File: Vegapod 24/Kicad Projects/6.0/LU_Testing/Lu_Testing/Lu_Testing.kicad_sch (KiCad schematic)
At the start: 101 parts, among them J1 DC Link, J2 OUT, J3 17V-35V IN, Q1 Q_NMOS_GDS, Q2 Q_NMOS_GDS, Q3 Q_PMOS_GSD, Q4 Q_PMOS_GSD, Q5 Q_PMOS_GSD, U1 LM7815_TO220, U2 KA78M05_TO252, U3 IR2110, U4 B0505S-1WR3, U5 LM324, U6 6N137, U7 6N137, U8 6N137

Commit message: LU PCB
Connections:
- net at C32.2, R37.1: now also U5.9 (-); no longer U5.6 (-)
- net at U5.10 (+): now also R38.1
- net at U5.5 (+): no longer R38.1
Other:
- moved on the sheet: U5B, U5C, U5D
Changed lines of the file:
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@@
+    (stroke (width 0) (type default) (color 0 0 0 0))
+  )
+  (wire (pts (xy 48.26 134.62) (xy 48.26 135.89))
     (stroke (width 0) (type default) (color 0 0 0 0))
   )
@@
     (stroke (width 0) (type default) (color 0 0 0 0))
   )
-  (wire (pts (xy 48.26 137.16) (xy 48.26 134.62))
-    (stroke (width 0) (type default) (color 0 0 0 0))
-  )
   (wire (pts (xy 38.1 156.21) (xy 34.29 156.21))
     (stroke (width 0) (type default) (color 0 0 0 0))
@@
   )
   (wire (pts (xy 173.99 67.31) (xy 173.99 74.93))
+    (stroke (width 0) (type default) (color 0 0 0 0))
+  )
+  (wire (pts (xy 48.26 132.08) (xy 48.26 130.81))
     (stroke (width 0) (type default) (color 0 0 0 0))
   )
@@
     (pin "2")
   )
-  (symbol (lib_id "Amplifier_Operational:LM324") (at 74.93 146.05 0) (unit 3)
-    (in_bom yes) (on_board yes) (fields_autoplaced)
-    (property "Reference" "U5" (id 0) (at 74.93 135.89 0))
-    (property "Value" "LM324" (id 1) (at 74.93 138.43 0))
-    (property "Footprint" "Package_SO:SOIC-14_3.9x8.7mm_P1.27mm" (id 2) (at 73.66 143.51 0)
-      (effects (font (size 1.27 1.27)) hide)
-    )
-    (property "Datasheet" "http://www.ti.com/lit/ds/symlink/lm2902-n.pdf" (id 3) (at 76.2 140.97 0)
+  (symbol (lib_id "Amplifier_Operational:LM324") (at 55.88 133.35 0) (unit 3)
+    (in_bom yes) (on_board yes) (fields_autoplaced)
+    (property "Reference" "U5" (id 0) (at 55.88 123.19 0))
+    (property "Value" "LM324" (id 1) (at 55.88 125.73 0))
+    (property "Footprint" "Package_SO:SOIC-14_3.9x8.7mm_P1.27mm" (id 2) (at 54.61 130.81 0)
+      (effects (font (size 1.27 1.27)) hide)
+    )
+    (property "Datasheet" "http://www.ti.com/lit/ds/symlink/lm2902-n.pdf" (id 3) (at 57.15 128.27 0)
       (effects (font (size 1.27 1.27)) hide)
     )
@@
     (pin "2")
   )
-  (symbol (lib_id "Amplifier_Operational:LM324") (at 100.33 139.7 0) (unit 4)
-    (in_bom yes) (on_board yes) (fields_autoplaced)
-    (property "Reference" "U5" (id 0) (at 100.33 129.54 0))
-    (property "Value" "LM324" (id 1) (at 100.33 132.08 0))
-    (property "Footprint" "Package_SO:SOIC-14_3.9x8.7mm_P1.27mm" (id 2) (at 99.06 137.16 0)
-      (effects (font (size 1.27 1.27)) hide)
-    )
-    (property "Datasheet" "http://www.ti.com/lit/ds/symlink/lm2902-n.pdf" (id 3) (at 101.6 134.62 0)
+  (symbol (lib_id "Amplifier_Operational:LM324") (at 85.09 133.35 0) (unit 4)
+    (in_bom yes) (on_board yes) (fields_autoplaced)
+    (property "Reference" "U5" (id 0) (at 85.09 123.19 0))
+    (property "Value" "LM324" (id 1) (at 85.09 125.73 0))
+    (property "Footprint" "Package_SO:SOIC-14_3.9x8.7mm_P1.27mm" (id 2) (at 83.82 130.81 0)
+      (effects (font (size 1.27 1.27)) hide)
+    )
+    (property "Datasheet" "http://www.ti.com/lit/ds/symlink/lm2902-n.pdf" (id 3) (at 86.36 128.27 0)
       (effects (font (size 1.27 1.27)) hide)
     )
@@
     (pin "2")
   )
-  (symbol (lib_id "Amplifier_Operational:LM324") (at 55.88 134.62 0) (unit 2)
-    (in_bom yes) (on_board yes) (fields_autoplaced)
-    (property "Reference" "U5" (id 0) (at 55.88 124.46 0))
-    (property "Value" "LM324" (id 1) (at 55.88 127 0))
-    (property "Footprint" "Package_SO:SOIC-14_3.9x8.7mm_P1.27mm" (id 2) (at 54.61 132.08 0)
-      (effects (font (size 1.27 1.27)) hide)
-    )
-    (property "Datasheet" "http://www.ti.com/lit/ds/symlink/lm2902-n.pdf" (id 3) (at 57.15 129.54 0)
-      (effects (font (size 1.27 1.27)) hide)
-    )
+  (symbol (lib_id "Amplifier_Operational:LM324") (at 31.75 123.19 0) (unit 2)
+    (in_bom yes) (on_board yes) (fields_autoplaced)
+    (property "Reference" "U5" (id 0) (at 31.75 113.03 0))
+    (property "Value" "LM324" (id 1) (at 31.75 115.57 0))
+    (property "Footprint" "Package_SO:SOIC-14_3.9x8.7mm_P1.27mm" (id 2) (at 30.48 120.65 0)
+      (effects (font (size 1.27 1.27)) hide)
+    )
+    (property "Datasheet" "http://www.ti.com/lit/ds/symlink/lm2902-n.pdf" (id 3) (at 33.02 118.11 0)
+      (effects (font (size 1.27 1.27)) hide)
+    )

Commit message: Power side complete lu
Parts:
- added C33, C34, C35, C37, C38: 100n, Capacitor_SMD:C_0805_2012Metric_Pad1.18x1.45mm_HandSolder, symbol Device:C_Small
- added C36, C39: 10u, Capacitor_SMD:C_1206_3216Metric_Pad1.33x1.80mm_HandSolder, symbol Device:C_Small
- added U10: ADUM4195-1BRIZ, ADUM4195-1:RI-8-1_ADI, symbol ADUM4195-1:ADUM4195-1BRIZ
- added U9: 6N137, Package_DIP:DIP-8_W7.62mm, symbol Isolator:6N137
- renumbered C11 to C1, C20 to C10, C5 to C11, C10 to C12, C8 to C13, C13 to C14, C17 to C15, C21 to C16, C6 to C17, C24 to C18, C14 to C19, C12 to C2, C1 to C20, C25 to C21, C2 to C23, C3 to C24, C23 to C25, C31 to C26, C26 to C27, C27 to C28, C28 to C29, C18 to C3, C29 to C30, C30 to C31, C9 to C5, C15 to C6, C19 to C7, C7 to C8, C16 to C9, D5 to D1, D6 to D2, D1 to D3, D8 to D4, D2 to D5, D4 to D6, D3 to D7, D7 to D8, J3 to J2, J2 to J3, R10 to R1, R20 to R10, R4 to R11, R26 to R12, R21 to R13, R28 to R14, R29 to R15, R30 to R16, R23 to R17, R1 to R18, R2 to R19, R13 to R2, R5 to R20, R6 to R21, R7 to R22, R8 to R23, R9 to R24, R12 to R25, R15 to R26, R18 to R27, R27 to R28, R24 to R29, R16 to R3, R39 to R30, R25 to R31, R40 to R32, R38 to R33, R37 to R34, R31 to R35, R34 to R36, R32 to R37, R35 to R38, R33 to R39, R19 to R4, R36 to R40, R22 to R5, R11 to R6, R14 to R7, R17 to R8, R3 to R9, U2 to U1, U1 to U2, U4 to U3, U3 to U4
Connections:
- net +5V: now also C33.1, C34.1, C35.1, C36.2, C37.2, U10.1 (VDD2)
- net A0: now also U10.2 (VIN)
- net GNDPWR: now also C33.2, C34.2, C35.2, C36.1, C37.1, U10.3 (SHTD), U10.4 (GND2), U9.3 (C)
- net CO: now reaches U5.8
- net CO: now also U9.2 (A)
- new net: C38.2, C39.2, U10.5 (GND1), U10.6 (NC)
- new net: C38.1, C39.1, U10.8 (VDD1)

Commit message: LU testing board
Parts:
- added C35: 47n, Capacitor_SMD:C_0805_2012Metric_Pad1.18x1.45mm_HandSolder, symbol Device:C_Small
- added R39: 220, Resistor_SMD:R_0805_2012Metric_Pad1.20x1.40mm_HandSolder, symbol Device:R
- added U9: STM32G474RET6, STM32G4:QFP50P1200X1200X160-64N, symbol STM32G4:STM32G474RET6
- renumbered C35 to C36, C36 to C37, C37 to C38, C38 to C39, C39 to C40, R39 to R40, R40 to R41, U9 to U10, U10 to U11
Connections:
- net DHIN: now reaches U7.2 (A)
- net DHIN: now also U9.8 (PC0)
- net GNDD: now reaches U7.3 (C)
- net GNDD: now also C39.2, C40.2, U10.5 (GND), U11.5 (GND1), U11.6 (NC), U6.3 (C), U8.3 (C), C35.1, U9.15 (VSS), U9.27 (VSSA), U9.31 (VSS), U9.47 (VSS), U9.63 (VSS)
- net DA0: now reaches U11.7 (VOUT)
- net DA0: now also U9.12 (PA0)
- net +5VD: now reaches C39.1, C40.1, U11.8 (VDD1)
- net +5VD: now also U10.7 (EN), U10.8 (VCC)
- net DPWMADJ: now reaches U6.2 (A)
- net DPWMADJ: now also U9.20 (PA6)
- net DLIN: now reaches U8.2 (A)
- net DLIN: now also U9.2 (PC13)
- net DFB: now reaches U10.6 (VO)
- net DFB: now also U9.24 (PB0)
- new net: C35.2, R39.1, U9.29 (VDDA)
- new net +3.3V: R39.2, U9.1 (VBAT), U9.16 (VDD), U9.32 (VDD), U9.48 (VDD), U9.64 (VDD)
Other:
- moved on the sheet: C37, C38, C39, C40, U11

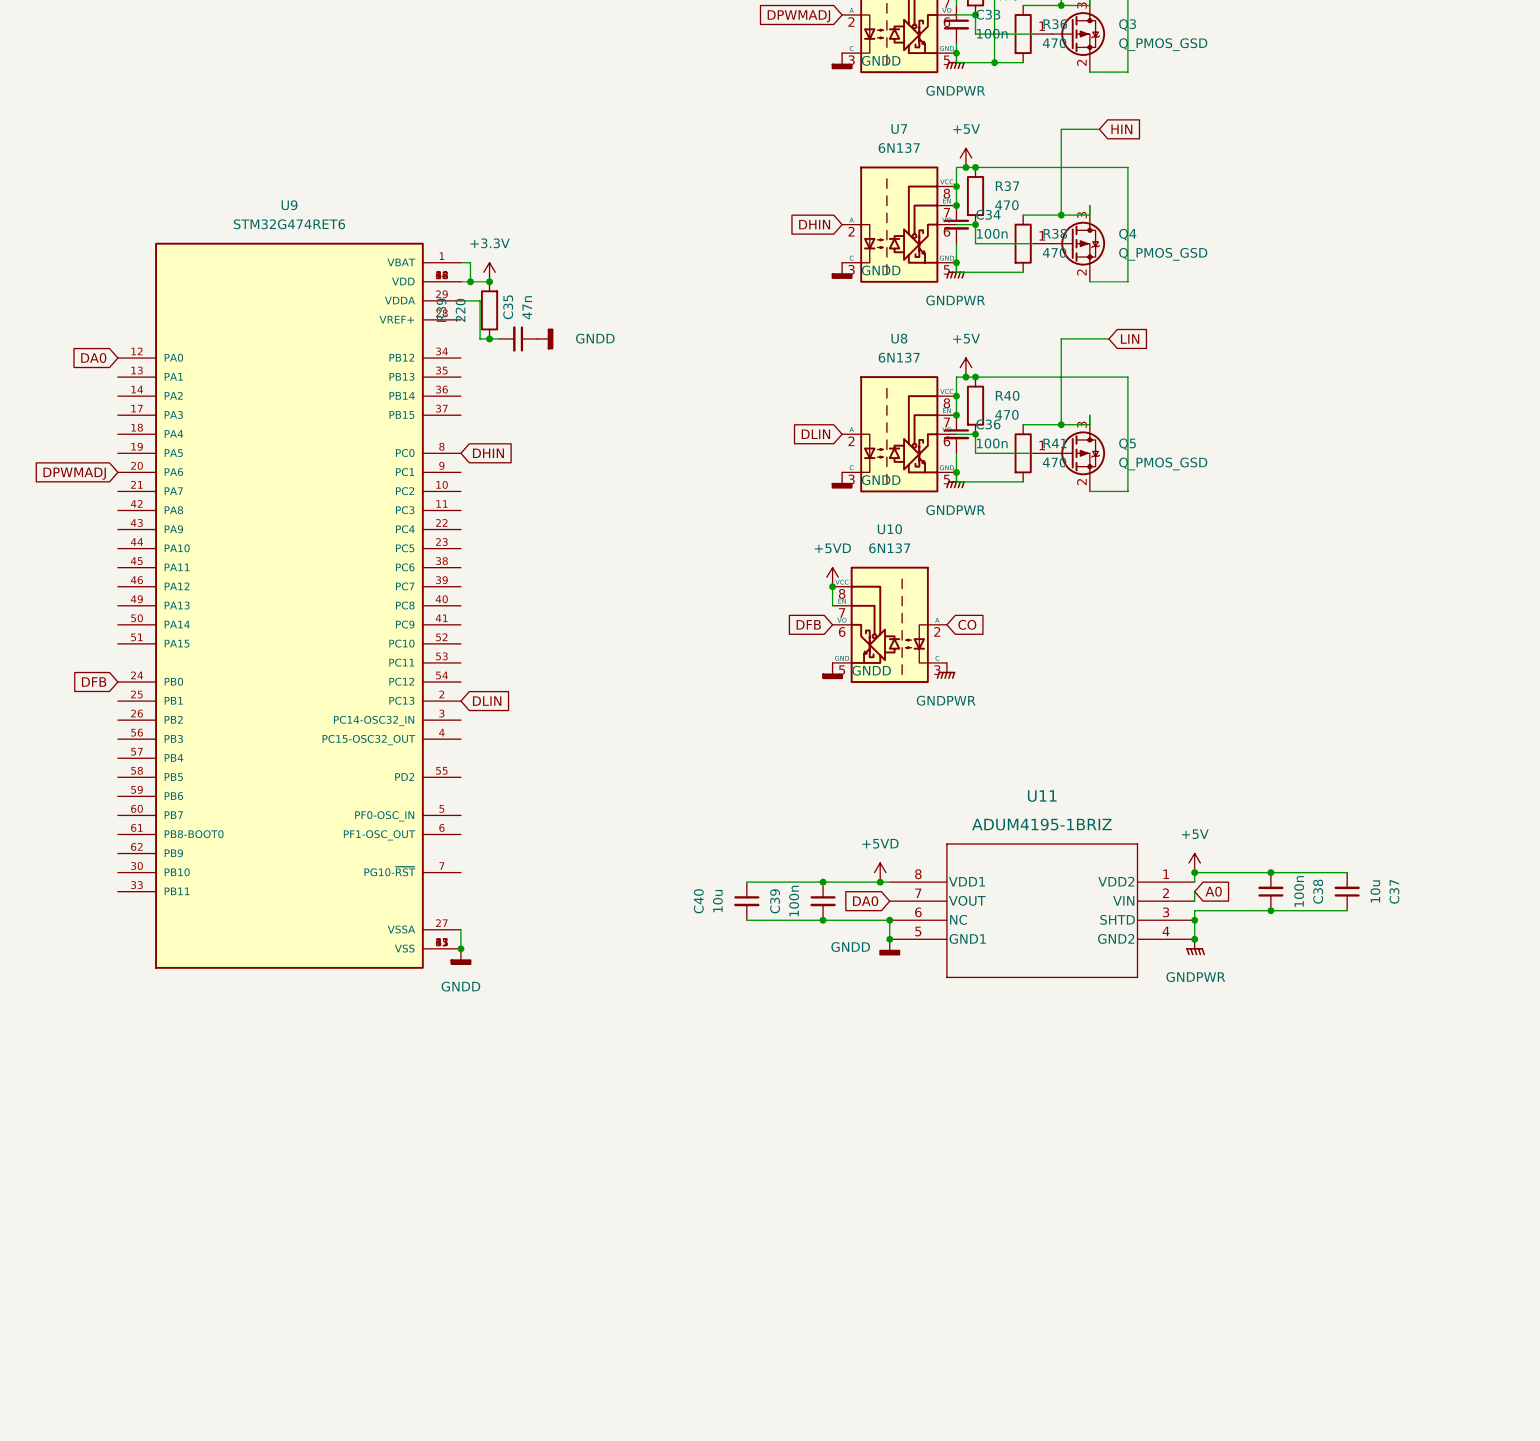
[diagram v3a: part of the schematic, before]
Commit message: UART and stlink missing lu board
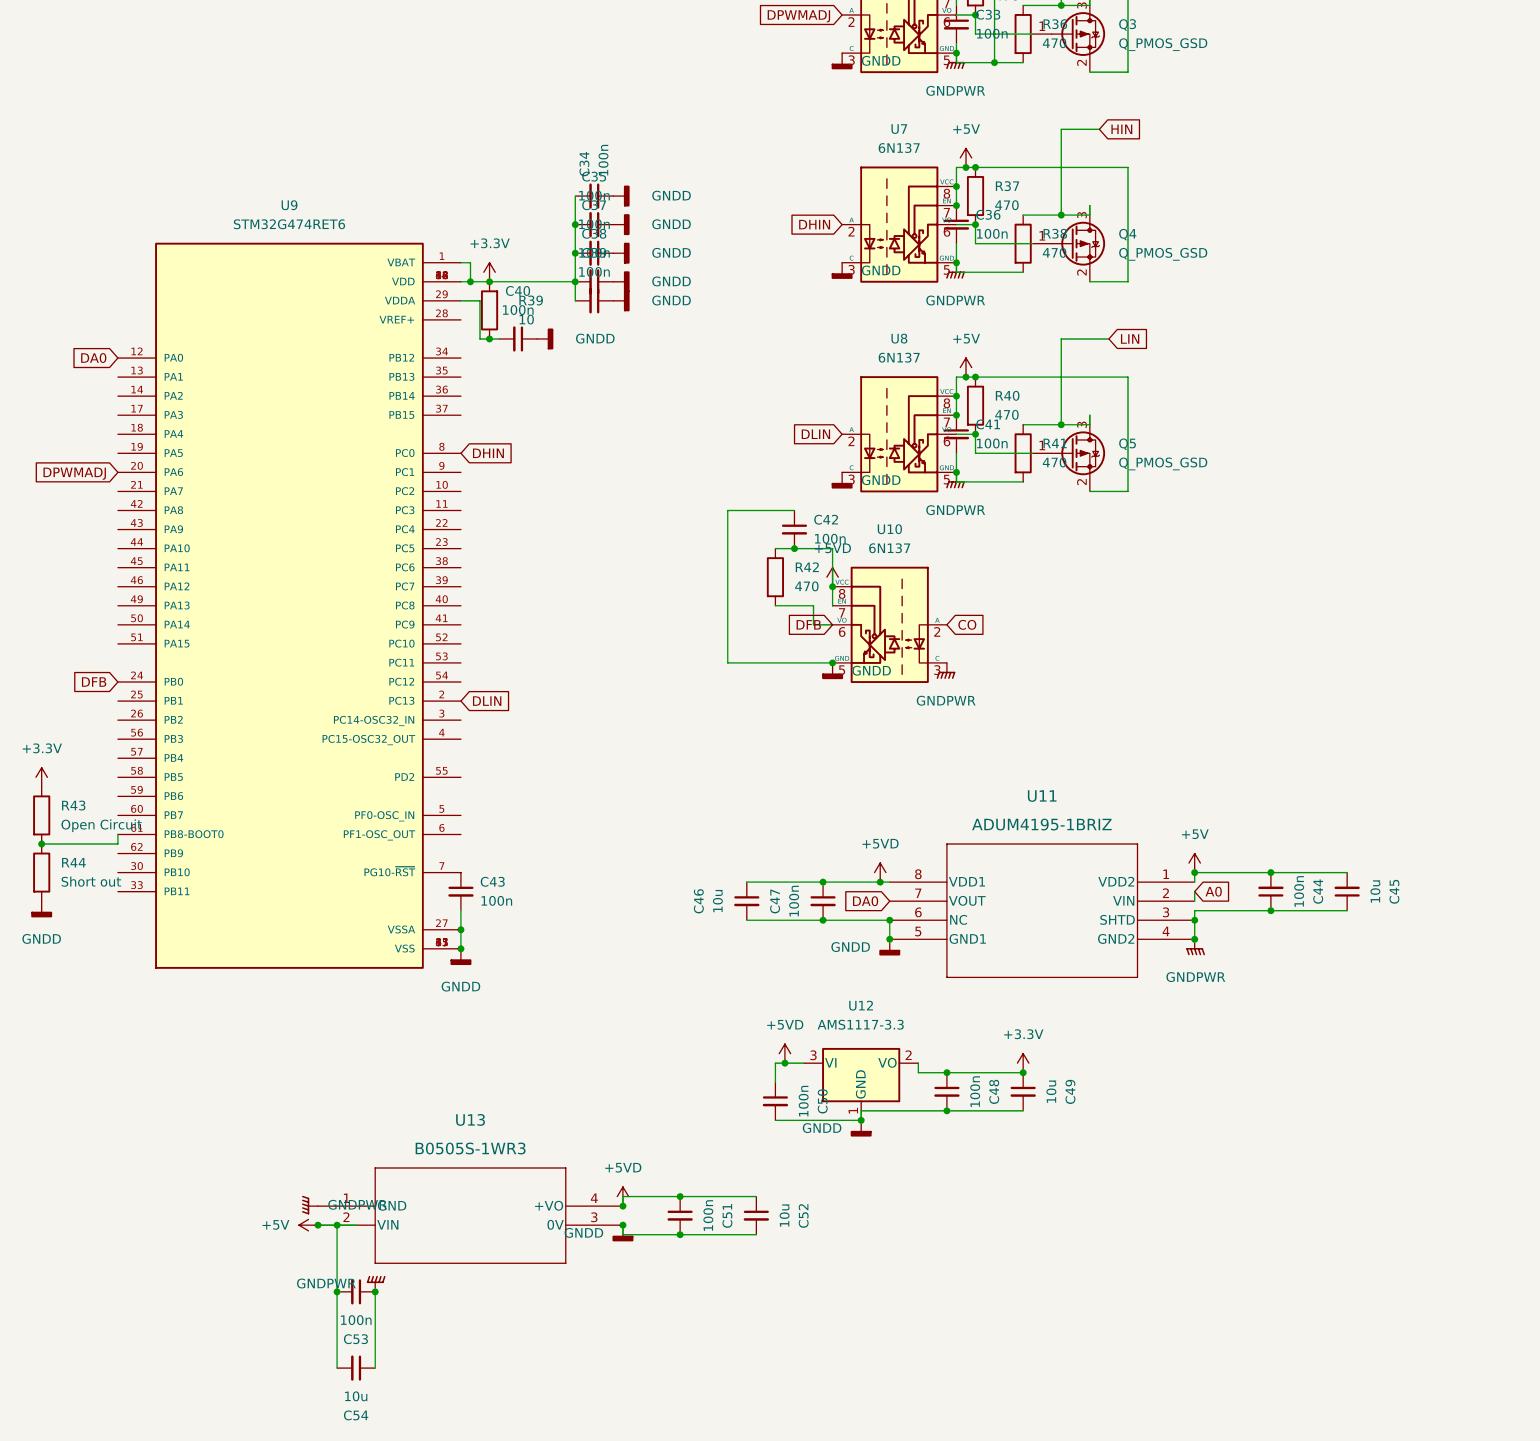
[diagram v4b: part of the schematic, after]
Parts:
- added C34, C35, C37, C38, C39, C42, C43, C48, C50, C51, C53: 100n, Capacitor_SMD:C_0805_2012Metric_Pad1.18x1.45mm_HandSolder, symbol Device:C_Small
- added C49, C52, C54: 10u, Capacitor_SMD:C_1206_3216Metric_Pad1.33x1.80mm_HandSolder, symbol Device:C_Small
- added R42: 470, Resistor_SMD:R_0805_2012Metric_Pad1.20x1.40mm_HandSolder, symbol Device:R
- added R43: Open Circuit, Resistor_SMD:R_0805_2012Metric_Pad1.20x1.40mm_HandSolder, symbol Device:R
- added R44: Short out, Resistor_SMD:R_0805_2012Metric_Pad1.20x1.40mm_HandSolder, symbol Device:R
- added U12: AMS1117-3.3, Package_TO_SOT_SMD:SOT-223-3_TabPin2, symbol Regulator_Linear:AMS1117-3.3
- added U13: B0505S-1WR3, B0505S-1WR3:B0505S_MNS, symbol B0505S-1WR3:B0505S-1WR3
- C40: renamed from C35; value 47n -> 100n
- R39: value 220 -> 10
- renumbered C34 to C36, C36 to C41, C38 to C44, C37 to C45, C40 to C46, C39 to C47
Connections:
- net +3.3V: now also C34.2, C35.2, C37.2, C38.2, C39.2, C48.1, C49.1, R43.1, U12.2 (VO)
- net +5V: now also C53.2, C54.2, U13.2 (VIN)
- net +5VD: now also C42.2, C50.1, C51.1, C52.1, R42.1, U12.3 (VI), U13.4 (+VO)
- net DFB: now also R42.2
- net GNDD: now also C34.1, C35.1, C37.1, C38.1, C39.1, C42.1, C43.2, C48.2, C49.2, C50.2, C51.2, C52.2, R44.2, U12.1 (GND), U13.3 (0V)
- net GNDPWR: now also C53.1, C54.1, U13.1 (GND)
- net at U9.61 (PB8-BOOT0): now also R43.2, R44.1
- net at U9.7 (PG10-~{RST}): now also C43.1
